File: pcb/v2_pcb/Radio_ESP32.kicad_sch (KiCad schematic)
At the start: 16 parts, among them J800 ESP UART PROGRAM (pin 1 VTREF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, SW800 RESET, SW801 BOOT, U800 ESP32-C6-MINI-1

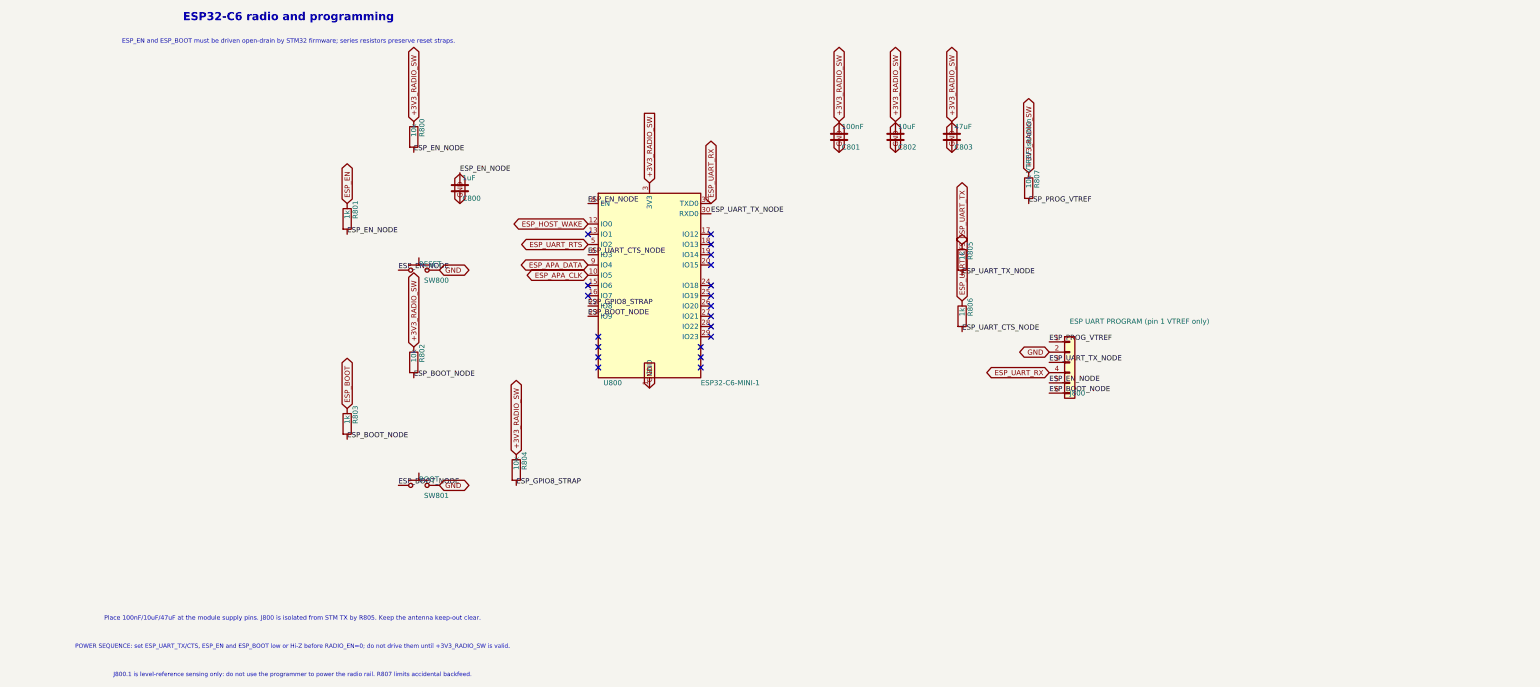
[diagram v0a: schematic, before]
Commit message: switch mosfets
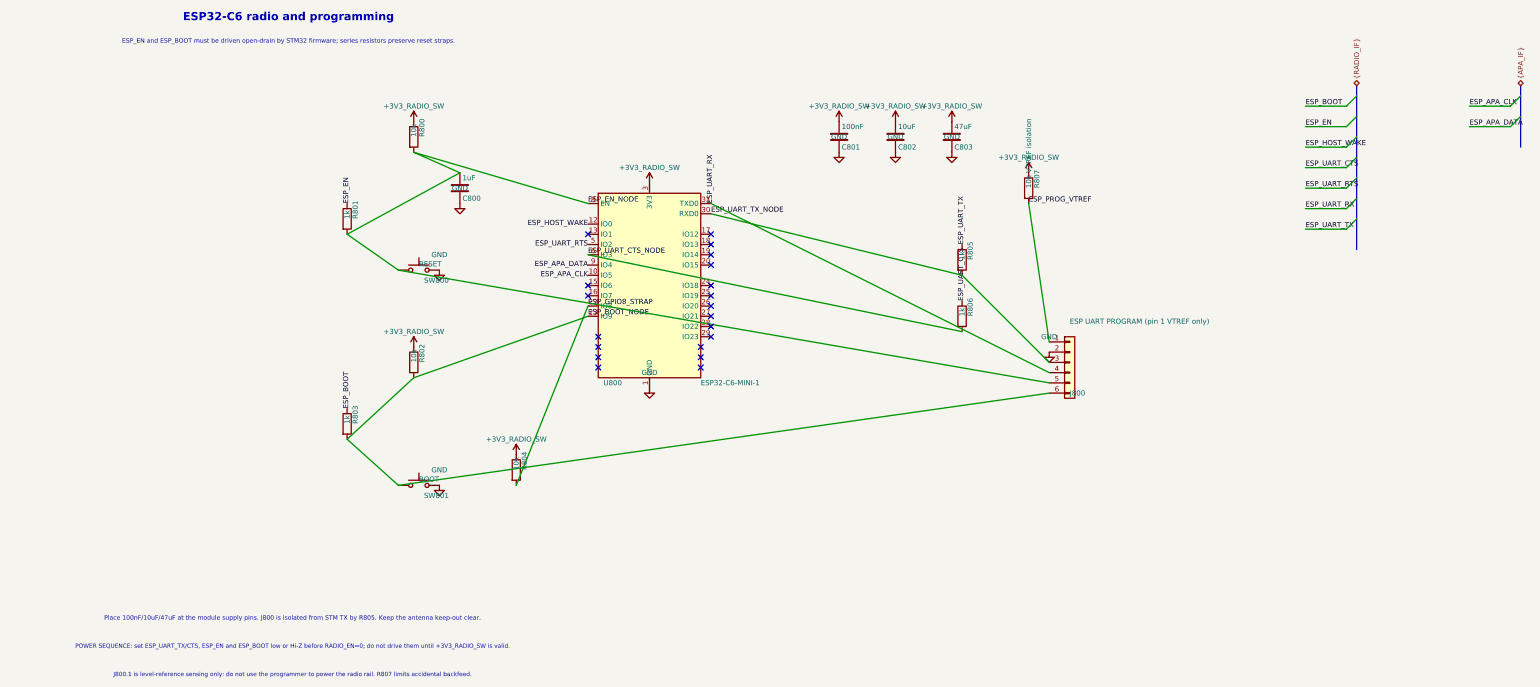
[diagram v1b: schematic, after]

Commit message: minor fixes
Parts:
- C800: value 1uF -> 1uF 25V X7R; Dielectric (none) -> X7R; MPN (none) -> CGA3E1X7R1E105K080AE; Manufacturer (none) -> TDK; Qualification (none) -> AEC-Q200; Termination (none) -> Soft termination; Tolerance (none) -> ±10%; Voltage (none) -> 25 VDC
- C801: value 100nF -> 100nF 50V X7R; Dielectric (none) -> X7R; MPN (none) -> CGA2B3X7R1H104K050BE; Manufacturer (none) -> TDK; Qualification (none) -> AEC-Q200; Termination (none) -> Soft termination; Tolerance (none) -> ±10%; Voltage (none) -> 50 VDC
- C802: value 10uF -> 10uF 10V X7R; Dielectric (none) -> X7R; MPN (none) -> GCJ21BR71A106KE01L; Manufacturer (none) -> Murata; Qualification (none) -> AEC-Q200; Termination (none) -> Soft termination; Tolerance (none) -> ±10%; Voltage (none) -> 10 VDC
- C803: value 47uF -> 47uF 10V X7R; footprint Capacitor_SMD:C_0805_2012Metric -> Capacitor_SMD:C_1210_3225Metric; Dielectric (none) -> X7R; MPN (none) -> C1210X476K8RACAUTO; Manufacturer (none) -> KEMET (Yageo Group); Qualification (none) -> AEC-Q200; Release_Status (none) -> Verify effective capacitance under worst-case DC bias; Termination (none) -> FT-CAP flexible termination; Tolerance (none) -> ±10%; Voltage (none) -> 10 VDC
- J800: value ESP UART PROGRAM (pin 1 VTREF only) -> M50-3530642 (VTREF sense only); MPN (none) -> M50-3530642; Manufacturer (none) -> Harwin; Notes (none) -> Unpolarized 1x6 header; retain strong pin-1 mark; pin 1 VTR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
- R800, R802, R804, R807: MPN (none) -> CRCW040210K0FKED; Manufacturer (none) -> Vishay; Power (none) -> 0.063 W; TCR (none) -> ±100 ppm/K; Tolerance (none) -> ±1%
- R801, R803, R805, R806: MPN (none) -> CRCW04021K00FKED; Manufacturer (none) -> Vishay; Power (none) -> 0.063 W; TCR (none) -> ±100 ppm/K; Tolerance (none) -> ±1%
- SW800: value RESET -> KMR223NG ULC LFG; Contact (none) -> Gold ULC; 1 µA minimum at 1.8 V; MPN KMR221GLFS -> Y78B22324FP; Manufacturer C&K -> Littelfuse (C&K); Operating_Temperature (none) -> -40 to +125 °C
- SW801: value BOOT -> KMR223NG ULC LFG; Contact (none) -> Gold ULC; 1 µA minimum at 1.8 V; MPN KMR221GLFS -> Y78B22324FP; Manufacturer C&K -> Littelfuse (C&K); Operating_Temperature (none) -> -40 to +125 °C
